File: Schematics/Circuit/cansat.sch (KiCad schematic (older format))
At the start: 32 parts, among them IC2 NCP1117ST33T3G, IC3 NCP1117ST50T3G

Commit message: Edit schematic and model
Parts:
- C1, C10, C17, C18, C19, C2, C20, C22, C24, C3, C4, C5, C6, C7, C8, C9: symbol C -> C-RESCUE-cansat
- R1, R2, R3, R4, R7: symbol R -> R-RESCUE-cansat
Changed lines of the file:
@@
 EESchema Schematic File Version 2
+LIBS:cansat-rescue
 LIBS:power
 LIBS:device
@@
 LIBS:memory
 LIBS:xilinx
-LIBS:special
 LIBS:microcontrollers
 LIBS:dsp
@@
 LIBS:contrib
 LIBS:valves
-LIBS:others
 LIBS:cansat
 LIBS:Relay
 LIBS:cansat-cache
-EELAYER 27 0
+EELAYER 25 0
 EELAYER END
 $Descr A4 11693 8268
@@
 $EndComp
 $Comp
-L C C1
+L C-RESCUE-cansat C1
 U 1 1 5A1AB74A
 P 3300 2450
@@
 $EndComp
 $Comp
-L C C2
+L C-RESCUE-cansat C2
 U 1 1 5A1AB807
 P 3300 1850
@@
 $EndComp
 $Comp
-L R R1
+L R-RESCUE-cansat R1
 U 1 1 5A1AB895
 P 3950 2150
@@
 $EndComp
 $Comp
-L GND #PWR?
+L GND-RESCUE-cansat #PWR?
 U 1 1 5A1AB907
 P 2850 2150
@@
 $EndComp
 $Comp
-L GND #PWR?
+L GND-RESCUE-cansat #PWR?
 U 1 1 5A1ABDEB
 P 3400 1550
@@
 $EndComp
 $Comp
-L C C3
+L C-RESCUE-cansat C3
 U 1 1 5A1ABE1A
 P 3000 1200
@@
 $EndComp
 $Comp
-L C C4
+L C-RESCUE-cansat C4
 U 1 1 5A1ABE29
 P 3800 1200
@@
 $EndComp
 $Comp
-L R R2
+L R-RESCUE-cansat R2
 U 1 1 5A1AC5F9
 P 1150 2100
@@
 $EndComp
 $Comp
-L C C5
+L C-RESCUE-cansat C5
 U 1 1 5A1AC62C
 P 1150 2650
@@
 $EndComp
 $Comp
-L GND #PWR?
+L GND-RESCUE-cansat #PWR?
 U 1 1 5A1AC74E
 P 1150 2850
@@
 SDA
 $Comp
-L R R4
+L R-RESCUE-cansat R4
 U 1 1 5A1ACFDA
 P 1400 3250
@@
 $EndComp
 $Comp
-L R R3
+L R-RESCUE-cansat R3
 U 1 1 5A1ACFE9
 P 1400 3450
@@
 SDA
 $Comp
-L +3.3V #PWR?
+L +3.3V-RESCUE-cansat #PWR?
 U 1 1 5A1B0206
 P 1750 3350
@@
 $EndComp
 $Comp
-L C C5
+L C-RESCUE-cansat C5
 U 1 1 5A1B02BD
 P 1050 1200
@@
 $EndComp
 $Comp
-L C C6
+L C-RESCUE-cansat C6
 U 1 1 5A1B02C3
 P 1850 1200
@@
 $EndComp
 $Comp
-L GND #PWR?
+L GND-RESCUE-cansat #PWR?
 U 1 1 5A1B02C9
 P 1450 1500
@@
 $EndComp
 $Comp
-L +3.3V #PWR?
+L +3.3V-RESCUE-cansat #PWR?
 U 1 1 5A1B02D7
 P 1850 600
@@
 $EndComp
 $Comp
-L C C7
+L C-RESCUE-cansat C7
 U 1 1 5A1B0F9C
 P 10950 900
@@
 $EndComp
 $Comp
-L GND #PWR?
+L GND-RESCUE-cansat #PWR?
 U 1 1 5A1B0FEF
 P 10950 700
@@
 $EndComp
 $Comp
-L GND #PWR?
+L GND-RESCUE-cansat #PWR?
 U 1 1 5A1B0FFE
 P 10950 1350
@@
 $EndComp
 $Comp
-L +3.3V #PWR?
+L +3.3V-RESCUE-cansat #PWR?
 U 1 1 5A1B1053
 P 10950 1850
@@
 $EndComp
 $Comp
-L +3.3V #PWR?
+L +3.3V-RESCUE-cansat #PWR?
 U 1 1 5A1B10A9
 P 8200 1450
@@
 $EndComp
 $Comp
-L C C8
+L C-RESCUE-cansat C8
 U 1 1 5A1B1100
 P 8450 1650
@@
 $EndComp
 $Comp
-L GND #PWR?
+L GND-RESCUE-cansat #PWR?
 U 1 1 5A1B110F
 P 8150 1650
@@
 SCL
 $Comp
-L GND #PWR?
+L GND-RESCUE-cansat #PWR?
 U 1 1 5A1B1343
 P 8150 750
@@
 $EndComp
 $Comp
-L C C10
+L C-RESCUE-cansat C10
 U 1 1 5A1B13EA
 P 10850 1600
@@
 $EndComp
 $Comp
-L R R7
+L R-RESCUE-cansat R7
 U 1 1 5A1B1509
 P 8500 2000
@@
 XTAL1
 $Comp
-L C C9
+L C-RESCUE-cansat C9
 U 1 1 5A1B12B6
 P 8250 1250
@@
 $EndComp
 $Comp
-L C C17
+L C-RESCUE-cansat C17
 U 1 1 5A28F703
 P 4950 1250
@@
 $EndComp
 $Comp
-L C C18
+L C-RESCUE-cansat C18
 U 1 1 5A28FA69
 P 5250 1250
@@
 $EndComp
 $Comp
-L C C19
+L C-RESCUE-cansat C19
 U 1 1 5A28FA6F
 P 5550 1250
@@
 $EndComp
 $Comp
-L C C20
+L C-RESCUE-cansat C20
 U 1 1 5A28FA75
 P 5850 1250
@@
 $EndComp
 $Comp
-L C C22
+L C-RESCUE-cansat C22
 U 1 1 5A3E3494
 P 2100 1200
@@
 $EndComp
 $Comp
-L C C24
+L C-RESCUE-cansat C24
 U 1 1 5A3E34A6
 P 4050 1200
@@
 $EndComp
 $Comp
-L GND #PWR?
+L GND-RESCUE-cansat #PWR?
 U 1 1 5A3E45AF
 P 5850 1000
@@
 $EndComp
 $Comp
-L GND #PWR?
+L GND-RESCUE-cansat #PWR?
 U 1 1 5A3E49E1
 P 5700 7400
@@
 $EndComp
 $Comp
-L GND #PWR?
+L GND-RESCUE-cansat #PWR?
 U 1 1 5A4B9C80
 P 10250 2400
@@
 $EndComp
 $Comp
-L GND #PWR?
+L GND-RESCUE-cansat #PWR?
 U 1 1 5A4BC235
 P 8450 2650
@@
 $EndComp
 $Comp
-L +3.3V #PWR?
+L +3.3V-RESCUE-cansat #PWR?
 U 1 1 5A4BC244
 P 9800 2450
@@
 $EndComp
 $Comp
-L GND #PWR?
+L GND-RESCUE-cansat #PWR?
 U 1 1 5A4BF903
 P 850 4100
@@
 $EndComp
 $Comp
-L GND #PWR?
+L GND-RESCUE-cansat #PWR?
 U 1 1 5A4BF91F
 P 850 4900

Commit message: Edit, add overall schematic, widen gaps in pcb
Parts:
- removed C1, C2, C5: 22 pF, ~, symbol C-RESCUE-cansat
- removed C10, C17, C18, C19, C20, C22, C24: 100 nF, ~, symbol C-RESCUE-cansat
- removed C3, C4, C5, C6: 47 uF, ~, symbol C-RESCUE-cansat
- removed C7: 2.2 nF, ~, symbol C-RESCUE-cansat
- removed C8: 0.8 uF, ~, symbol C-RESCUE-cansat
- removed C9: 10 nF, ~, symbol C-RESCUE-cansat
- removed CSTECE16M0V53-r0: 16MHZ, ~, symbol CRYSTAL
- removed D1: CD1206-S01575, ~, symbol DIODE
- removed IC2: NCP1117ST33T3G, symbol NCP1117ST50T3G
- removed IC3: NCP1117ST50T3G, symbol NCP1117ST50T3G
- removed IC?: ATMEGA2560-A, TQFP100, symbol ATMEGA2560-A
- removed IC?: MPU-6050, ~, symbol MPU-6050
- removed K? (x2): HESOP1, symbol HESOP1
- removed P?: CONN_O2, symbol CONN_4
- removed P?: CONN_3X2, symbol CONN_3X2
- removed R1: 1M, ~, symbol R-RESCUE-cansat
- removed R2, R3, R4: 10k, ~, symbol R-RESCUE-cansat
- removed R7: 4k7, ~, symbol R-RESCUE-cansat
- added C? (x4): 100nF, Capacitors_SMD:C_0805, symbol C
- added C? (x4): 4.7uF, Capacitors_SMD:C_0402, symbol C
- added C? (x2): 0.22 uF, Capacitors_SMD:C_0402, symbol C-RESCUE-top
- added C? (x4): 100 nF, Capacitors_SMD:C_0805, symbol C-RESCUE-top
- added C?: 10 uF, Capacitors_SMD:C_0805, symbol C-RESCUE-top
- added C? (x2): 20 pF, Capacitors_SMD:C_0402, symbol C-RESCUE-main
- added C? (x3): 47 uF, Capacitors_Tantalum_SMD:CP_Tantalum_Case-C_EIA-6032-28_Reflow, symbol C-RESCUE-main
- added C?: 22 pF, Capacitors_SMD:C_0805, symbol C-RESCUE-main
- added C?: 47 uF, Capacitors_Tantalum_SMD:CP_Tantalum_Case-U_EIA-6032-15_Reflow, symbol C-RESCUE-main
- added C? (x7): 100 nF, Capacitors_SMD:C_0805, symbol C-RESCUE-main
- added CSTECE?: 16MHZ, CanSat:Crystal_SMD, symbol CRYSTAL
- added D? (x4): LED, Diodes_SMD:D_0603, symbol LED
- added D?: LED, Diodes_SMD:D_0603, symbol LED-RESCUE-top
- added D?: CD1206-S01575, Diodes_SMD:D_MiniMELF, symbol DIODE
- added IC? (x4): VL53L0X, VL53L0X:XDCR_VL53L0CXV0DH%2f1, symbol VL53L0X
- added IC?: HIH9131, SOIC127P600X175-8N:SOIC127P600X175-8N, symbol HIH9131
- added IC?: LPS22HB, LPS22HB:LGA10R50P2X3_200X200X80, symbol LPS22HB
- added IC?: NCP1117ST50T3G, CanSat:ncp1117, symbol NCP1117ST50T3G
- added IC?: NCP1117ST33T3G, CanSat:ncp1117, symbol NCP1117ST50T3G
- added IC?: ATMEGA2560-A, CanSat:AtMega2560-AU, symbol ATMEGA2560-A
- added IC?: RFM69HW, RFM69HW:XCVR_RFM95W-868S2, symbol RFM69HW
- added J? (x9): Conn_01x07, CanSat:MOLEX_PicoBlade_7, symbol Conn_01x07
- added J?: Conn_01x05, Pin_Headers:Pin_Header_Straight_1x05_Pitch1.27mm_SMD_Pin1Left, symbol Conn_01x05
- added J?: Conn_01x03, MOLEX_PicoBlade_3:MOLEX_0532610371, symbol Conn_01x03
- added J?: Conn_01x05, Pin_Headers:Pin_Header_Straight_1x05_Pitch1.27mm_SMD_Pin1Right, symbol Conn_01x05
- added J?: Conn_02x05_Counter_Clockwise, Pin_Headers:Pin_Header_Straight_2x05_Pitch1.00mm_SMD, symbol Conn_02x05_Counter_Clockwise
- added J?: Conn_01x06, CanSat:MOLEX_PicoBlade_6, symbol Conn_01x06
- added J? (x2): Conn_01x04, CanSat:MOLEX_PicoBlade_4, symbol Conn_01x04
- added K? (x2): HESOP1, CanSat:SMD_6pin_IC, symbol HESOP1
- added P?: CONN_O2, CanSat:MOLEX_PicoBlade_4, symbol CONN_4
- added P?: CONN_3X2, CanSat:co2, symbol CONN_3X2
- added P? (x19): CONN_2, CanSat:MOLEX_PicoBlade_2, symbol CONN_2
- added Q? (x6): BSS138, TO_SOT_Packages_SMD:SOT-23, symbol BSS138
- added R? (x5): 150, Resistors_SMD:R_0805, symbol R
- added R?: 1M, Resistors_SMD:R_0603, symbol R-RESCUE-main
- added R? (x2): 10k, Resistors_SMD:R_0603, symbol R-RESCUE-main
- added R? (x2): 2k, Resistors_SMD:R_0603, symbol R-RESCUE-main
- added R? (x4): 2k2, Resistors_SMD:R_0805, symbol R
- added R? (x4): 2k8, Resistors_SMD:R_0603, symbol R
- added R? (x20): 10k, Resistors_SMD:R_0603, symbol R
- added R?: 20k, Resistors_SMD:R_0603, symbol R-RESCUE-main
- added U?: LSM303AGRTR, CanSat:LSM303AGRTR, symbol LSM303AGRTR
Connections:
- net labels added: DTR, INT, INT1, INT2, INT3, INT4, LED, LED1, LED2, LED3, LED4, LED_TOP, MISO, MOSI, PWM1, PWM2, PWM3, PWM4, PWM5, PWM6, PWM7, PWM8, PWRKEY, RFMINT, RFM_INT, RXD-GSM, RX_GPS, SCK, SERVO, SLEEP-GSM, SS, TXD-GSM, TX_GPS, V_READ, XSHUT, XSHUT1, XSHUT2, XSHUT3, XSHUT4
- wire segments 77 -> 391
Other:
- note added: "Arm1"
- note added: "Arm2\n"
- note added: "Arm3"
- note added: "Arm4"
- note added: "Main Board"
- note added: "Top Board"

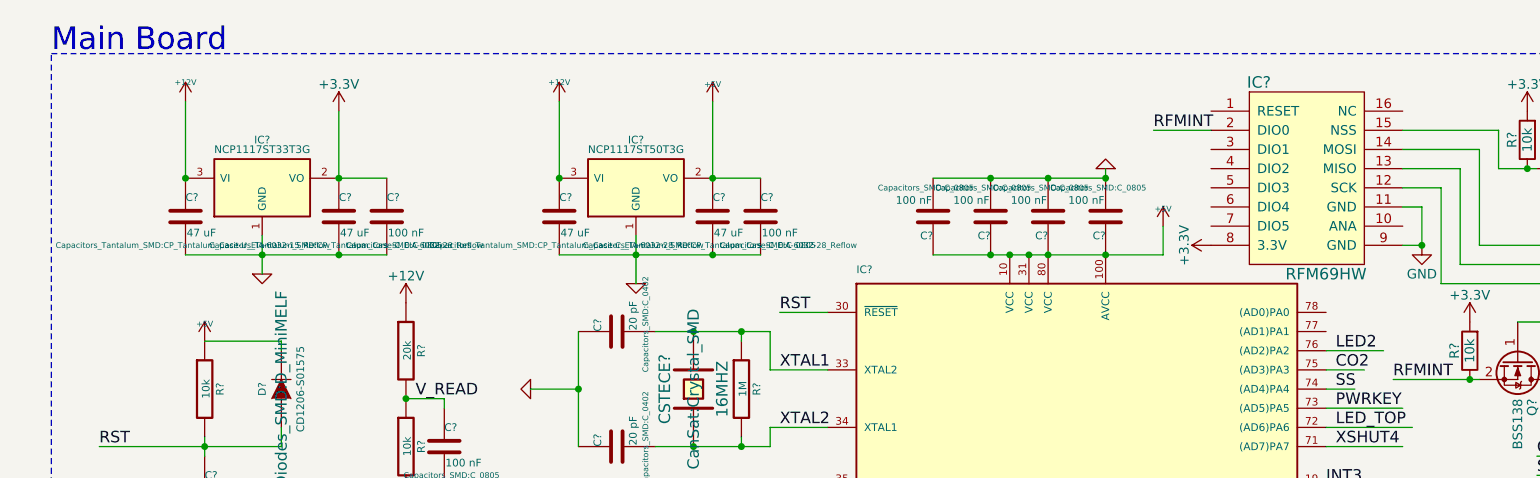
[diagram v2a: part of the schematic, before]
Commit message: Edit schematic and model, add images
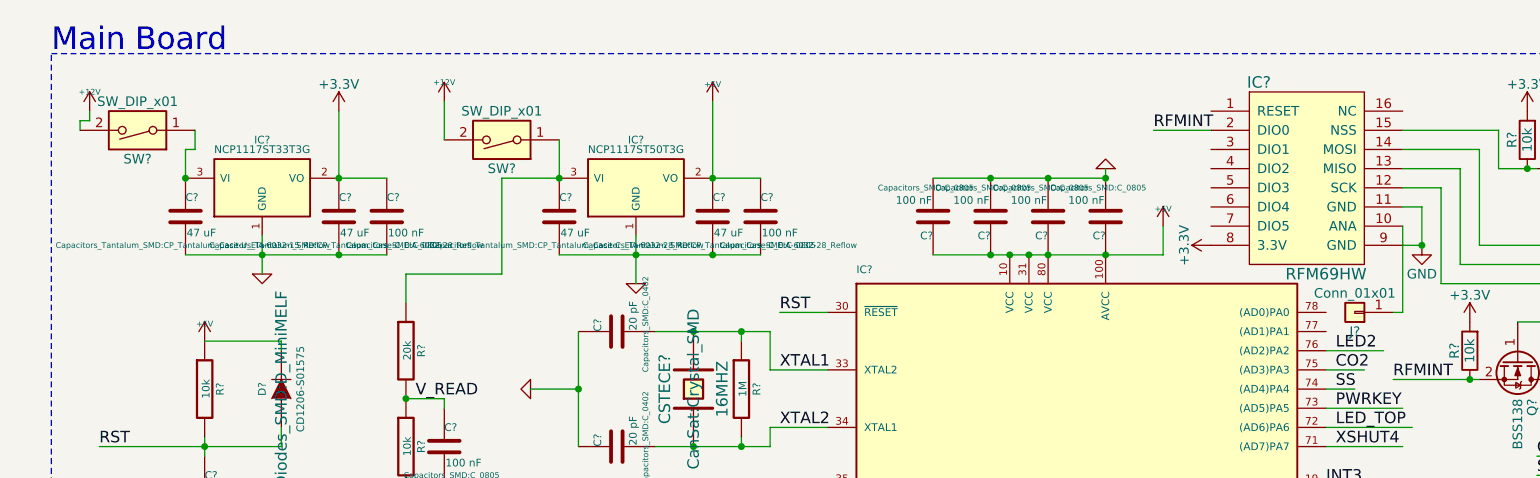
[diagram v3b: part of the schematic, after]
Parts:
- removed C? (x2): 20 pF, Capacitors_SMD:C_0402, symbol C-RESCUE-main
- removed C? (x3): 47 uF, Capacitors_Tantalum_SMD:CP_Tantalum_Case-C_EIA-6032-28_Reflow, symbol C-RESCUE-main
- removed C?: 22 pF, Capacitors_SMD:C_0805, symbol C-RESCUE-main
- removed C?: 47 uF, Capacitors_Tantalum_SMD:CP_Tantalum_Case-U_EIA-6032-15_Reflow, symbol C-RESCUE-main
- removed C? (x7): 100 nF, Capacitors_SMD:C_0805, symbol C-RESCUE-main
- removed CSTECE?: 16MHZ, CanSat:Crystal_SMD, symbol CRYSTAL
- removed D?: CD1206-S01575, Diodes_SMD:D_MiniMELF, symbol DIODE
- removed IC?: NCP1117ST50T3G, CanSat:ncp1117, symbol NCP1117ST50T3G
- removed IC?: NCP1117ST33T3G, CanSat:ncp1117, symbol NCP1117ST50T3G
- removed IC?: ATMEGA2560-A, CanSat:AtMega2560-AU, symbol ATMEGA2560-A
- removed IC?: RFM69HW, RFM69HW:XCVR_RFM95W-868S2, symbol RFM69HW
- removed J? (x5): Conn_01x07, CanSat:MOLEX_PicoBlade_7, symbol Conn_01x07
- removed J?: Conn_01x03, MOLEX_PicoBlade_3:MOLEX_0532610371, symbol Conn_01x03
- removed J?: Conn_01x05, Pin_Headers:Pin_Header_Straight_1x05_Pitch1.27mm_SMD_Pin1Right, symbol Conn_01x05
- removed J?: Conn_02x05_Counter_Clockwise, Pin_Headers:Pin_Header_Straight_2x05_Pitch1.00mm_SMD, symbol Conn_02x05_Counter_Clockwise
- removed J?: Conn_01x06, CanSat:MOLEX_PicoBlade_6, symbol Conn_01x06
- removed J? (x2): Conn_01x04, CanSat:MOLEX_PicoBlade_4, symbol Conn_01x04
- removed K? (x2): HESOP1, CanSat:SMD_6pin_IC, symbol HESOP1
- removed P?: CONN_O2, CanSat:MOLEX_PicoBlade_4, symbol CONN_4
- removed P?: CONN_3X2, CanSat:co2, symbol CONN_3X2
- removed P? (x19): CONN_2, CanSat:MOLEX_PicoBlade_2, symbol CONN_2
- removed Q? (x6): BSS138, TO_SOT_Packages_SMD:SOT-23, symbol BSS138
- removed R?: 1M, Resistors_SMD:R_0603, symbol R-RESCUE-main
- removed R? (x2): 10k, Resistors_SMD:R_0603, symbol R-RESCUE-main
- removed R? (x2): 2k, Resistors_SMD:R_0603, symbol R-RESCUE-main
- removed R? (x4): 2k2, Resistors_SMD:R_0805, symbol R
- removed R? (x4): 2k8, Resistors_SMD:R_0603, symbol R
- removed R? (x20): 10k, Resistors_SMD:R_0603, symbol R
- removed R?: 20k, Resistors_SMD:R_0603, symbol R-RESCUE-main
- added C? (x2): 20 pF, Capacitors_SMD:C_0402, symbol C-RESCUE-main
- added C? (x3): 47 uF, Capacitors_Tantalum_SMD:CP_Tantalum_Case-C_EIA-6032-28_Reflow, symbol C-RESCUE-main
- added C?: 22 pF, Capacitors_SMD:C_0805, symbol C-RESCUE-main
- added C?: 47 uF, Capacitors_Tantalum_SMD:CP_Tantalum_Case-U_EIA-6032-15_Reflow, symbol C-RESCUE-main
- added C? (x7): 100 nF, Capacitors_SMD:C_0805, symbol C-RESCUE-main
- added CSTECE?: 16MHZ, CanSat:Crystal_SMD, symbol CRYSTAL
- added D?: CD1206-S01575, Diodes_SMD:D_MiniMELF, symbol DIODE
- added IC?: NCP1117ST50T3G, CanSat:ncp1117, symbol NCP1117ST50T3G
- added IC?: NCP1117ST33T3G, CanSat:ncp1117, symbol NCP1117ST50T3G
- added IC?: ATMEGA2560-A, CanSat:AtMega2560-AU, symbol ATMEGA2560-A
- added IC?: RFM69HW, RFM69HW:XCVR_RFM95W-868S2, symbol RFM69HW
- added J? (x5): Conn_01x07, CanSat:MOLEX_PicoBlade_7, symbol Conn_01x07
- added J?: Conn_01x03, MOLEX_PicoBlade_3:MOLEX_0532610371, symbol Conn_01x03
- added J?: Conn_01x05, Pin_Headers:Pin_Header_Straight_1x05_Pitch1.27mm_SMD_Pin1Right, symbol Conn_01x05
- added J?: Conn_02x05_Counter_Clockwise, Pin_Headers:Pin_Header_Straight_2x05_Pitch1.00mm_SMD, symbol Conn_02x05_Counter_Clockwise
- added J?: Conn_01x06, CanSat:MOLEX_PicoBlade_6, symbol Conn_01x06
- added J? (x2): Conn_01x04, CanSat:MOLEX_PicoBlade_4, symbol Conn_01x04
- added J?: Conn_01x01, Pin_Headers:Pin_Header_Straight_1x01_Pitch2.54mm, symbol Conn_01x01
- added K? (x2): HESOP1, CanSat:SMD_6pin_IC, symbol HESOP1
- added P?: CONN_O2, CanSat:MOLEX_PicoBlade_4, symbol CONN_4
- added P?: CONN_3X2, CanSat:co2, symbol CONN_3X2
- added P? (x19): CONN_2, CanSat:MOLEX_PicoBlade_2, symbol CONN_2
- added Q? (x6): BSS138, TO_SOT_Packages_SMD:SOT-23, symbol BSS138
- added R?: 1M, Resistors_SMD:R_0603, symbol R-RESCUE-main
- added R? (x2): 10k, Resistors_SMD:R_0603, symbol R-RESCUE-main
- added R? (x2): 2k, Resistors_SMD:R_0603, symbol R-RESCUE-main
- added R? (x4): 2k2, Resistors_SMD:R_0805, symbol R
- added R? (x4): 2k8, Resistors_SMD:R_0603, symbol R
- added R? (x20): 10k, Resistors_SMD:R_0603, symbol R
- added R?: 20k, Resistors_SMD:R_0603, symbol R-RESCUE-main
- added SW? (x2): SW_DIP_x01, CanSat:Switch, symbol SW_DIP_x01
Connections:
- wire segments 391 -> 403
